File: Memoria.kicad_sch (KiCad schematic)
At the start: 135 parts, among them J1 RGB Breakout, J2 Hull LED Breakout, U1 PRTR5V0U2X, U2 ATmega32U4-MUR, Y1 16MHz

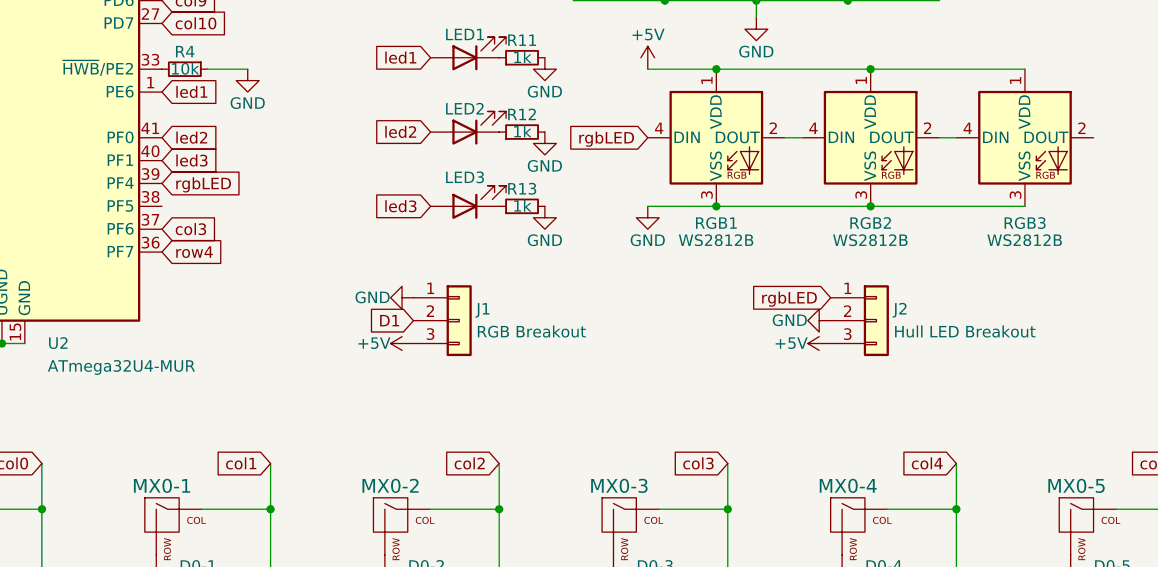
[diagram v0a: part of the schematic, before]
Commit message: the final final pass
silkscreen art, added 470 resistor, changed 1uF capacitor in BOM
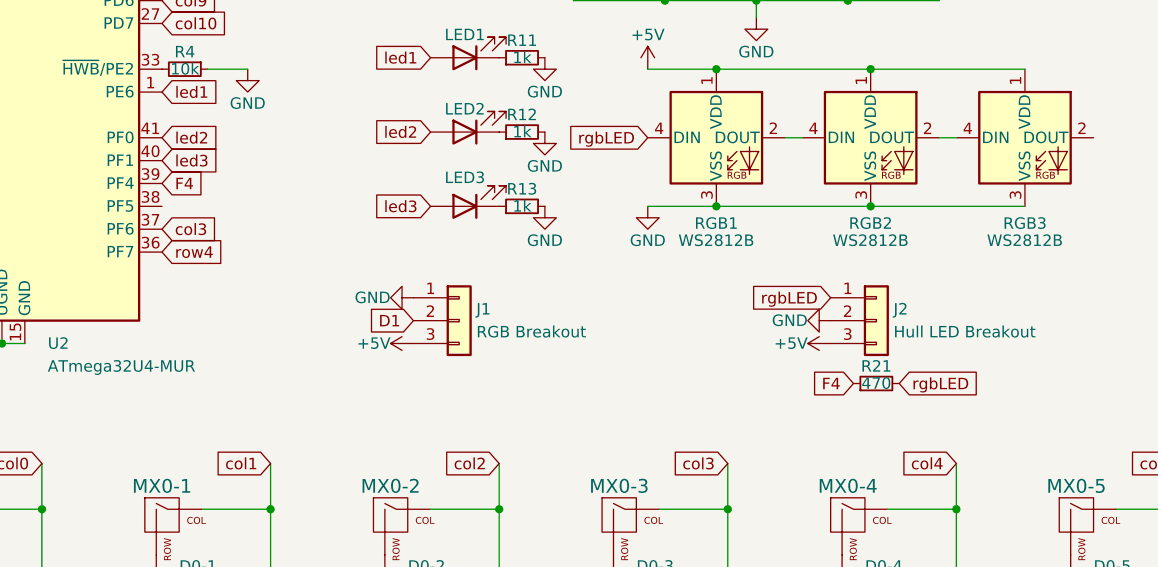
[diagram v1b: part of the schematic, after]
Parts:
- added R21: 470, Resistor_SMD:R_0805_2012Metric, symbol Device:R_Small
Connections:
- net rgbLED: now also R21.2; no longer U2.39 (PF4)
- new net F4: R21.1, U2.39 (PF4)
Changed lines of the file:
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@@
     )
   )
+  (global_label "rgbLED" (shape input) (at 150.495 123.19 0) (fields_autoplaced)
+    (effects (font (size 1.27 1.27)) (justify left))
+    (property "Intersheet References" "${INTERSHEET_REFS}" (id 0) (at 159.3506 123.2694 0)
+      (effects (font (size 1.27 1.27)) (justify left) hide)
+    )
+  )
   (global_label "D1" (shape input) (at 68.58 67.945 0) (fields_autoplaced)
     (effects (font (size 1.27 1.27)) (justify left))
@@
     )
   )
-  (global_label "rgbLED" (shape input) (at 68.58 100.965 0) (fields_autoplaced)
+  (global_label "F4" (shape input) (at 68.58 100.965 0) (fields_autoplaced)
     (effects (font (size 1.27 1.27)) (justify left))
-    (property "Intersheet References" "${INTERSHEET_REFS}" (id 0) (at 77.4356 101.0444 0)
+    (property "Intersheet References" "${INTERSHEET_REFS}" (id 0) (at 73.2023 100.8856 0)
       (effects (font (size 1.27 1.27)) (justify left) hide)
     )
@@
     )
   )
+  (global_label "F4" (shape input) (at 145.415 123.19 180) (fields_autoplaced)
+    (effects (font (size 1.27 1.27)) (justify right))
+    (property "Intersheet References" "${INTERSHEET_REFS}" (id 0) (at 140.7927 123.2694 0)
+      (effects (font (size 1.27 1.27)) (justify right) hide)
+    )
+  )
   (global_label "col10" (shape input) (at 309.245 157.48 180) (fields_autoplaced)
     (effects (font (size 1.27 1.27)) (justify right))
@@
   (symbol (lib_id "power:+5V") (at 142.875 118.745 90) (unit 1)
     (in_bom yes) (on_board yes)
-    (property "Reference" "#PWR?" (id 0) (at 146.685 118.745 0)
+    (property "Reference" "#PWR0131" (id 0) (at 146.685 118.745 0)
       (effects (font (size 1.27 1.27)) hide)
     )
@@
   (symbol (lib_id "power:GND") (at 142.875 116.205 270) (unit 1)
     (in_bom yes) (on_board yes)
-    (property "Reference" "#PWR?" (id 0) (at 136.525 116.205 0)
+    (property "Reference" "#PWR0132" (id 0) (at 136.525 116.205 0)
       (effects (font (size 1.27 1.27)) hide)
     )
@@
     (pin "2")
   )
+  (symbol (lib_id "Device:R_Small") (at 147.955 123.19 90) (unit 1)
+    (in_bom yes) (on_board yes)
+    (property "Reference" "R21" (id 0) (at 147.955 121.285 90))
+    (property "Value" "470" (id 1) (at 147.955 123.19 90))
+    (property "Footprint" "Resistor_SMD:R_0805_2012Metric" (id 2) (at 147.955 123.19 0)
+      (effects (font (size 1.27 1.27)) hide)
+    )
+    (property "Datasheet" "~" (id 3) (at 147.955 123.19 0)
+      (effects (font (size 1.27 1.27)) hide)
+    )
+    (pin "1")
+    (pin "2")
+  )
   (symbol (lib_id "Device:D_Small") (at 194.945 170.18 90) (unit 1)
     (in_bom yes) (on_board yes)
@@
     )
     (path "/5cc3461a-45b6-4b27-ab8b-a723e63abeac"
-      (reference "#PWR?") (unit 1) (value "+5V") (footprint "")
+      (reference "#PWR0131") (unit 1) (value "+5V") (footprint "")
     )
     (path "/8361155d-68f9-4145-b719-cc4650ce0993"
-      (reference "#PWR?") (unit 1) (value "GND") (footprint "")
+      (reference "#PWR0132") (unit 1) (value "GND") (footprint "")
     )
     (path "/2bcaec8d-d053-42b7-8b2c-efbbb5891c05"
@@
       (reference "R13") (unit 1) (value "1k") (footprint "Resistor_SMD:R_0805_2012Metric")
     )
+    (path "/b7a5e1fe-ecd2-416f-8c50-0882654e2cb1"
+      (reference "R21") (unit 1) (value "470") (footprint "Resistor_SMD:R_0805_2012Metric")
+    )
     (path "/239b8b6d-a04e-4b46-9919-bcf2d3615097"

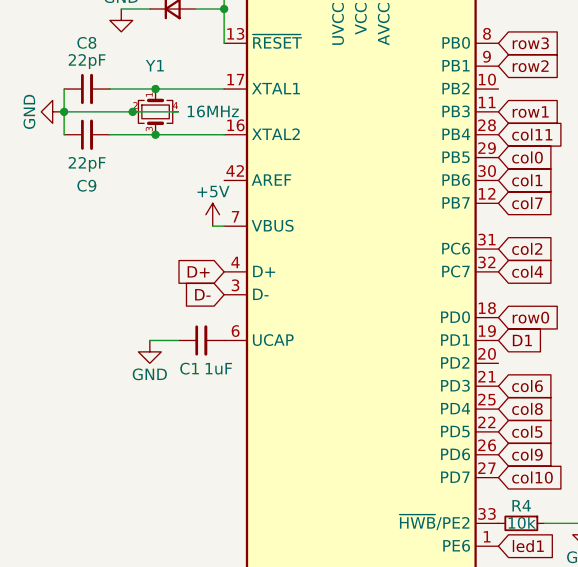
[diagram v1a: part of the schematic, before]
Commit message: added termination resistors
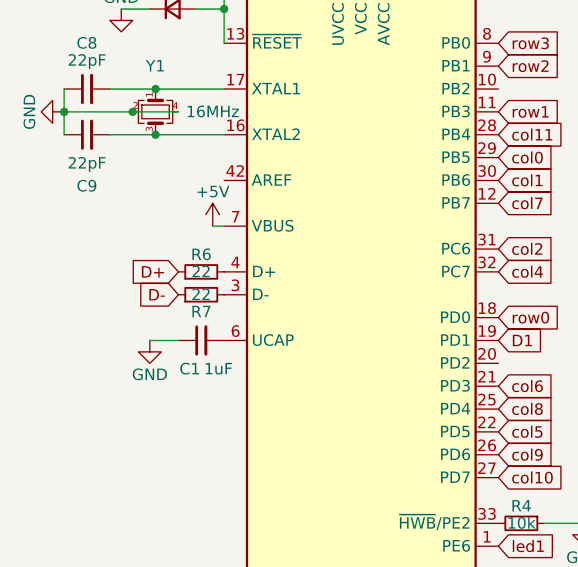
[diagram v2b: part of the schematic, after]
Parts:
- added R6, R7: 22, Resistor_SMD:R_0805_2012Metric, symbol Device:R_Small
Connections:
- net D+: now also R6.1; no longer U2.4 (D+)
- net D-: now also R7.1; no longer U2.3 (D-)
- new net: R6.2, U2.4 (D+)
- new net: R7.2, U2.3 (D-)
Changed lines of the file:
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@@
     )
   )
-  (global_label "D-" (shape input) (at 38.1 62.865 180) (fields_autoplaced)
+  (global_label "D-" (shape input) (at 33.02 62.865 180) (fields_autoplaced)
     (effects (font (size 1.27 1.27)) (justify right))
-    (property "Intersheet References" "${INTERSHEET_REFS}" (id 0) (at 32.8445 62.7856 0)
+    (property "Intersheet References" "${INTERSHEET_REFS}" (id 0) (at 27.7645 62.7856 0)
       (effects (font (size 1.27 1.27)) (justify right) hide)
     )
   )
-  (global_label "D+" (shape input) (at 38.1 60.325 180) (fields_autoplaced)
+  (global_label "D+" (shape input) (at 33.02 60.325 180) (fields_autoplaced)
     (effects (font (size 1.27 1.27)) (justify right))
-    (property "Intersheet References" "${INTERSHEET_REFS}" (id 0) (at 32.8445 60.2456 0)
+    (property "Intersheet References" "${INTERSHEET_REFS}" (id 0) (at 27.7645 60.2456 0)
       (effects (font (size 1.27 1.27)) (justify right) hide)
     )
@@
     (pin "2")
   )
+  (symbol (lib_id "Device:R_Small") (at 35.56 60.325 90) (unit 1)
+    (in_bom yes) (on_board yes)
+    (property "Reference" "R6" (id 0) (at 35.56 58.42 90))
+    (property "Value" "22" (id 1) (at 35.56 60.325 90))
+    (property "Footprint" "Resistor_SMD:R_0805_2012Metric" (id 2) (at 35.56 60.325 0)
+      (effects (font (size 1.27 1.27)) hide)
+    )
+    (property "Datasheet" "~" (id 3) (at 35.56 60.325 0)
+      (effects (font (size 1.27 1.27)) hide)
+    )
+    (pin "1")
+    (pin "2")
+  )
   (symbol (lib_id "Device:D_Small") (at 144.145 246.38 90) (unit 1)
     (in_bom yes) (on_board yes)
@@
     (pin "2")
   )
+  (symbol (lib_id "Device:R_Small") (at 35.56 62.865 90) (unit 1)
+    (in_bom yes) (on_board yes)
+    (property "Reference" "R7" (id 0) (at 35.56 64.77 90))
+    (property "Value" "22" (id 1) (at 35.56 62.865 90))
+    (property "Footprint" "Resistor_SMD:R_0805_2012Metric" (id 2) (at 35.56 62.865 0)
+      (effects (font (size 1.27 1.27)) hide)
+    )
+    (property "Datasheet" "~" (id 3) (at 35.56 62.865 0)
+      (effects (font (size 1.27 1.27)) hide)
+    )
+    (pin "1")
+    (pin "2")
+  )
   (symbol (lib_id "MX_Alps_Hybrid:MX-NoLED") (at 145.415 240.03 0) (unit 1)
     (in_bom yes) (on_board yes)
@@
       (reference "R5") (unit 1) (value "1M") (footprint "Resistor_SMD:R_0603_1608Metric")
     )
+    (path "/42589805-d870-4e5e-a7a4-a45895232563"
+      (reference "R6") (unit 1) (value "22") (footprint "Resistor_SMD:R_0805_2012Metric")
+    )
+    (path "/6118074d-2187-49f7-8bba-5145076ff0ec"
+      (reference "R7") (unit 1) (value "22") (footprint "Resistor_SMD:R_0805_2012Metric")
+    )
     (path "/fb67d14e-a15c-45fa-a4d4-50654be68d2c"
